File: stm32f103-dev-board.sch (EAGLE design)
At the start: 33 parts, among them Q1 8MHz, U1 STM32F103CBT6, U2 LM1117MP-3.3, Y1 32.768kHz

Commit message: v0.2
added led on PC13
added power led
added external power in
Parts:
- added D1, D2: (no value), SparkFun-LED:LED3MM
- added D3, D4: 1A/40V/500mV, SparkFun-DiscreteSemi:DIODE-SCHOTTKY-SS14
- added J5: (no value), SparkFun-Connectors:CONN_02
- added R1, R9: 470, rcl:R-EU_R0805
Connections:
- new net N$1: D3.A, X1.VBUS
- new net N$2: D2.A, R9.2
- new net N$3: D1.A, R1.2
- new net N$5: D4.A, J5.2
- net +3V3: now also R1.1
- net +5V: now also D3.C, D4.C; no longer X1.VBUS
- net GND: now also D1.C, D2.C, J5.1
- net PC13: now also R9.1
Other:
- note added: "Curious Mind http://acemielektronikci.blogspot.com"
- note added: "v0.2"
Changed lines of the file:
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@@
 <layer number="28" name="bValues" color="7" fill="1" visible="yes" active="no"/>
 <layer number="29" name="tStop" color="7" fill="3" visible="no" active="no"/>
-<layer number="30" name="bStop" color="7" fill="6" visible="no" active="no"/>
+<layer number="30" name="bStop" color="7" fill="1" visible="no" active="no"/>
 <layer number="31" name="tCream" color="7" fill="4" visible="no" active="no"/>
 <layer number="32" name="bCream" color="7" fill="5" visible="no" active="no"/>
@@
 <part name="J6" library="SparkFun-Connectors" deviceset="CONN_11" device=""/>
 <part name="J4" library="SparkFun-Connectors" deviceset="CONN_12" device=""/>
-<part name="FRAME1" library="SparkFun-Aesthetics" deviceset="FRAME-LETTER" device=""/>
+<part name="R1" library="rcl" deviceset="R-EU_" device="R0805" value="470"/>
+<part name="R9" library="rcl" deviceset="R-EU_" device="R0805" value="470"/>
+<part name="D1" library="SparkFun-LED" deviceset="LED" device="3MM"/>
+<part name="D2" library="SparkFun-LED" deviceset="LED" device="3MM"/>
+<part name="+3V4" library="supply1" deviceset="+3V3" device=""/>
+<part name="GND8" library="supply1" deviceset="GND" device=""/>
+<part name="D3" library="SparkFun-DiscreteSemi" deviceset="DIODE-SCHOTTKY" device="-SS14" value="1A/40V/500mV"/>
+<part name="D4" library="SparkFun-DiscreteSemi" deviceset="DIODE-SCHOTTKY" device="-SS14" value="1A/40V/500mV"/>
+<part name="J5" library="SparkFun-Connectors" deviceset="CONN_02" device=""/>
+<part name="GND11" library="supply1" deviceset="GND" device=""/>
+<part name="FRAME1" library="SparkFun-Aesthetics" deviceset="FRAME-LETTER" device="" value="FRAME-LETTER"/>
 </parts>
 <sheets>
@@
 <plain>
 <text x="-12.7" y="30.48" size="1.27" layer="91">BOOT1</text>
+<text x="30.48" y="-67.31" size="2.54" layer="91" font="vector">           Curious Mind
+http://acemielektronikci.blogspot.com</text>
+<text x="115.57" y="-67.056" size="2.54" layer="91" font="vector">v0.2</text>
 </plain>
 <instances>
@@
 <attribute name="VALUE" x="109.22" y="-25.4" size="1.778" layer="96"/>
 </instance>
-<instance part="P+2" gate="1" x="-83.82" y="-48.26" smashed="yes" rot="R180">
-<attribute name="VALUE" x="-81.28" y="-43.18" size="1.778" layer="96" rot="R270"/>
+<instance part="P+2" gate="1" x="-63.5" y="-48.26" smashed="yes" rot="R270">
+<attribute name="VALUE" x="-68.58" y="-45.72" size="1.778" layer="96"/>
 </instance>
 <instance part="P+3" gate="1" x="30.48" y="-5.08" smashed="yes">
@@
 <attribute name="VALUE" x="119.38" y="108.966" size="1.778" layer="96" font="vector" rot="R180"/>
 <attribute name="NAME" x="119.38" y="73.152" size="1.778" layer="95" font="vector" rot="R180"/>
+</instance>
+<instance part="R1" gate="G$1" x="-68.58" y="22.86" smashed="yes" rot="R180">
+<attribute name="NAME" x="-64.77" y="21.3614" size="1.778" layer="95" rot="R180"/>
+<attribute name="VALUE" x="-64.77" y="26.162" size="1.778" layer="96" rot="R180"/>
+</instance>
+<instance part="R9" gate="G$1" x="-68.58" y="15.24" smashed="yes" rot="R180">
+<attribute name="NAME" x="-64.77" y="13.7414" size="1.778" layer="95" rot="R180"/>
+<attribute name="VALUE" x="-64.77" y="18.542" size="1.778" layer="96" rot="R180"/>
+</instance>
+<instance part="D1" gate="G$1" x="-78.74" y="22.86" smashed="yes" rot="R270">
+<attribute name="NAME" x="-83.312" y="26.289" size="1.778" layer="95" font="vector"/>
+<attribute name="VALUE" x="-83.312" y="20.955" size="1.778" layer="96" font="vector" align="top-left"/>
+</instance>
+<instance part="D2" gate="G$1" x="-78.74" y="15.24" smashed="yes" rot="R270">
+<attribute name="NAME" x="-83.312" y="18.669" size="1.778" layer="95" font="vector"/>
+<attribute name="VALUE" x="-83.312" y="13.335" size="1.778" layer="96" font="vector" align="top-left"/>
+</instance>
+<instance part="+3V4" gate="G$1" x="-58.42" y="27.94" smashed="yes">
+<attribute name="VALUE" x="-60.96" y="22.86" size="1.778" layer="96" rot="R90"/>
+</instance>
+<instance part="GND8" gate="1" x="-86.36" y="12.7" smashed="yes">
+<attribute name="VALUE" x="-88.9" y="10.16" size="1.778" layer="96"/>
+</instance>
+<instance part="D3" gate="G$1" x="-83.82" y="-43.18" smashed="yes">
+<attribute name="NAME" x="-86.36" y="-41.148" size="1.778" layer="95" font="vector"/>
+<attribute name="VALUE" x="-86.36" y="-45.212" size="1.778" layer="96" font="vector" align="top-left"/>
+</instance>
+<instance part="D4" gate="G$1" x="-83.82" y="-53.34" smashed="yes">
+<attribute name="NAME" x="-86.36" y="-51.308" size="1.778" layer="95" font="vector"/>
+<attribute name="VALUE" x="-86.36" y="-55.372" size="1.778" layer="96" font="vector" align="top-left"/>
+</instance>
+<instance part="J5" gate="G$1" x="-93.98" y="-55.88" smashed="yes">
+<attribute name="VALUE" x="-96.52" y="-60.706" size="1.778" layer="96" font="vector"/>
+<attribute name="NAME" x="-96.52" y="-50.292" size="1.778" layer="95" font="vector"/>
+</instance>
+<instance part="GND11" gate="1" x="-83.82" y="-60.96" smashed="yes">
+<attribute name="VALUE" x="-86.36" y="-63.5" size="1.778" layer="96"/>
 </instance>
 <instance part="FRAME1" gate="G$1" x="-121.92" y="-73.66" smashed="yes"/>
@@
 <pinref part="J4" gate="G$1" pin="11"/>
 <wire x1="109.22" y1="78.74" x2="91.44" y2="78.74" width="0.1524" layer="91"/>
+</segment>
+<segment>
+<pinref part="D1" gate="G$1" pin="C"/>
+<pinref part="GND8" gate="1" pin="GND"/>
+<wire x1="-83.82" y1="22.86" x2="-86.36" y2="22.86" width="0.1524" layer="91"/>
+<wire x1="-86.36" y1="22.86" x2="-86.36" y2="15.24" width="0.1524" layer="91"/>
+<pinref part="D2" gate="G$1" pin="C"/>
+<wire x1="-83.82" y1="15.24" x2="-86.36" y2="15.24" width="0.1524" layer="91"/>
+<junction x="-86.36" y="15.24"/>
+</segment>
+<segment>
+<pinref part="J5" gate="G$1" pin="1"/>
+<wire x1="-86.36" y1="-55.88" x2="-83.82" y2="-55.88" width="0.1524" layer="91"/>
+<pinref part="GND11" gate="1" pin="GND"/>
+<wire x1="-83.82" y1="-55.88" x2="-83.82" y2="-58.42" width="0.1524" layer="91"/>
 </segment>
 </net>
@@
 <label x="-93.98" y="78.74" size="1.778" layer="95"/>
 </segment>
+<segment>
+<pinref part="R1" gate="G$1" pin="1"/>
+<wire x1="-63.5" y1="22.86" x2="-58.42" y2="22.86" width="0.1524" layer="91"/>
+<pinref part="+3V4" gate="G$1" pin="+3V3"/>
+<wire x1="-58.42" y1="22.86" x2="-58.42" y2="25.4" width="0.1524" layer="91"/>
+</segment>
 </net>
 <net name="N$7" class="0">
@@
 </segment>
 <segment>
-<pinref part="X1" gate="G$1" pin="VBUS"/>
+<pinref part="D3" gate="G$1" pin="C"/>
+<wire x1="-81.28" y1="-43.18" x2="-66.04" y2="-43.18" width="0.1524" layer="91"/>
+<wire x1="-66.04" y1="-43.18" x2="-66.04" y2="-48.26" width="0.1524" layer="91"/>
+<pinref part="D4" gate="G$1" pin="C"/>
+<wire x1="-66.04" y1="-48.26" x2="-66.04" y2="-53.34" width="0.1524" layer="91"/>
+<wire x1="-66.04" y1="-53.34" x2="-81.28" y2="-53.34" width="0.1524" layer="91"/>
 <pinref part="P+2" gate="1" pin="+5V"/>
-<wire x1="-86.36" y1="-43.18" x2="-83.82" y2="-43.18" width="0.1524" layer="91"/>
-<wire x1="-83.82" y1="-43.18" x2="-83.82" y2="-45.72" width="0.1524" layer="91"/>
+<junction x="-66.04" y="-48.26"/>
 </segment>
 </net>
@@
 <wire x1="-104.14" y1="76.2" x2="-83.82" y2="76.2" width="0.1524" layer="91"/>
 <label x="-93.98" y="76.2" size="1.778" layer="95"/>
+</segment>
+<segment>
+<pinref part="R9" gate="G$1" pin="1"/>
+<wire x1="-63.5" y1="15.24" x2="-58.42" y2="15.24" width="0.1524" layer="91"/>
+<label x="-63.5" y="15.24" size="1.778" layer="95"/>
 </segment>
 </net>
@@
 </segment>
 </net>
+<net name="N$2" class="0">
+<segment>
+<pinref part="R9" gate="G$1" pin="2"/>
+<pinref part="D2" gate="G$1" pin="A"/>
+<wire x1="-73.66" y1="15.24" x2="-76.2" y2="15.24" width="0.1524" layer="91"/>
+</segment>
+</net>
+<net name="N$3" class="0">
+<segment>
+<pinref part="R1" gate="G$1" pin="2"/>
+<pinref part="D1" gate="G$1" pin="A"/>
+<wire x1="-73.66" y1="22.86" x2="-76.2" y2="22.86" width="0.1524" layer="91"/>
+</segment>
+</net>
+<net name="N$1" class="0">
+<segment>
+<pinref part="X1" gate="G$1" pin="VBUS"/>
+<pinref part="D3" gate="G$1" pin="A"/>
+</segment>
+</net>
+<net name="N$5" class="0">
+<segment>
+<pinref part="J5" gate="G$1" pin="2"/>
+<pinref part="D4" gate="G$1" pin="A"/>
+</segment>
+</net>
 </nets>
 </sheet>
@@
 </schematic>
 </drawing>
+<compatibility>
+<note version="6.3" minversion="6.2.2" severity="warning">
+Since Version 6.2.2 text objects can contain more than one line,
+which will not be processed correctly with this version.
+</note>
+</compatibility>
 </eagle>

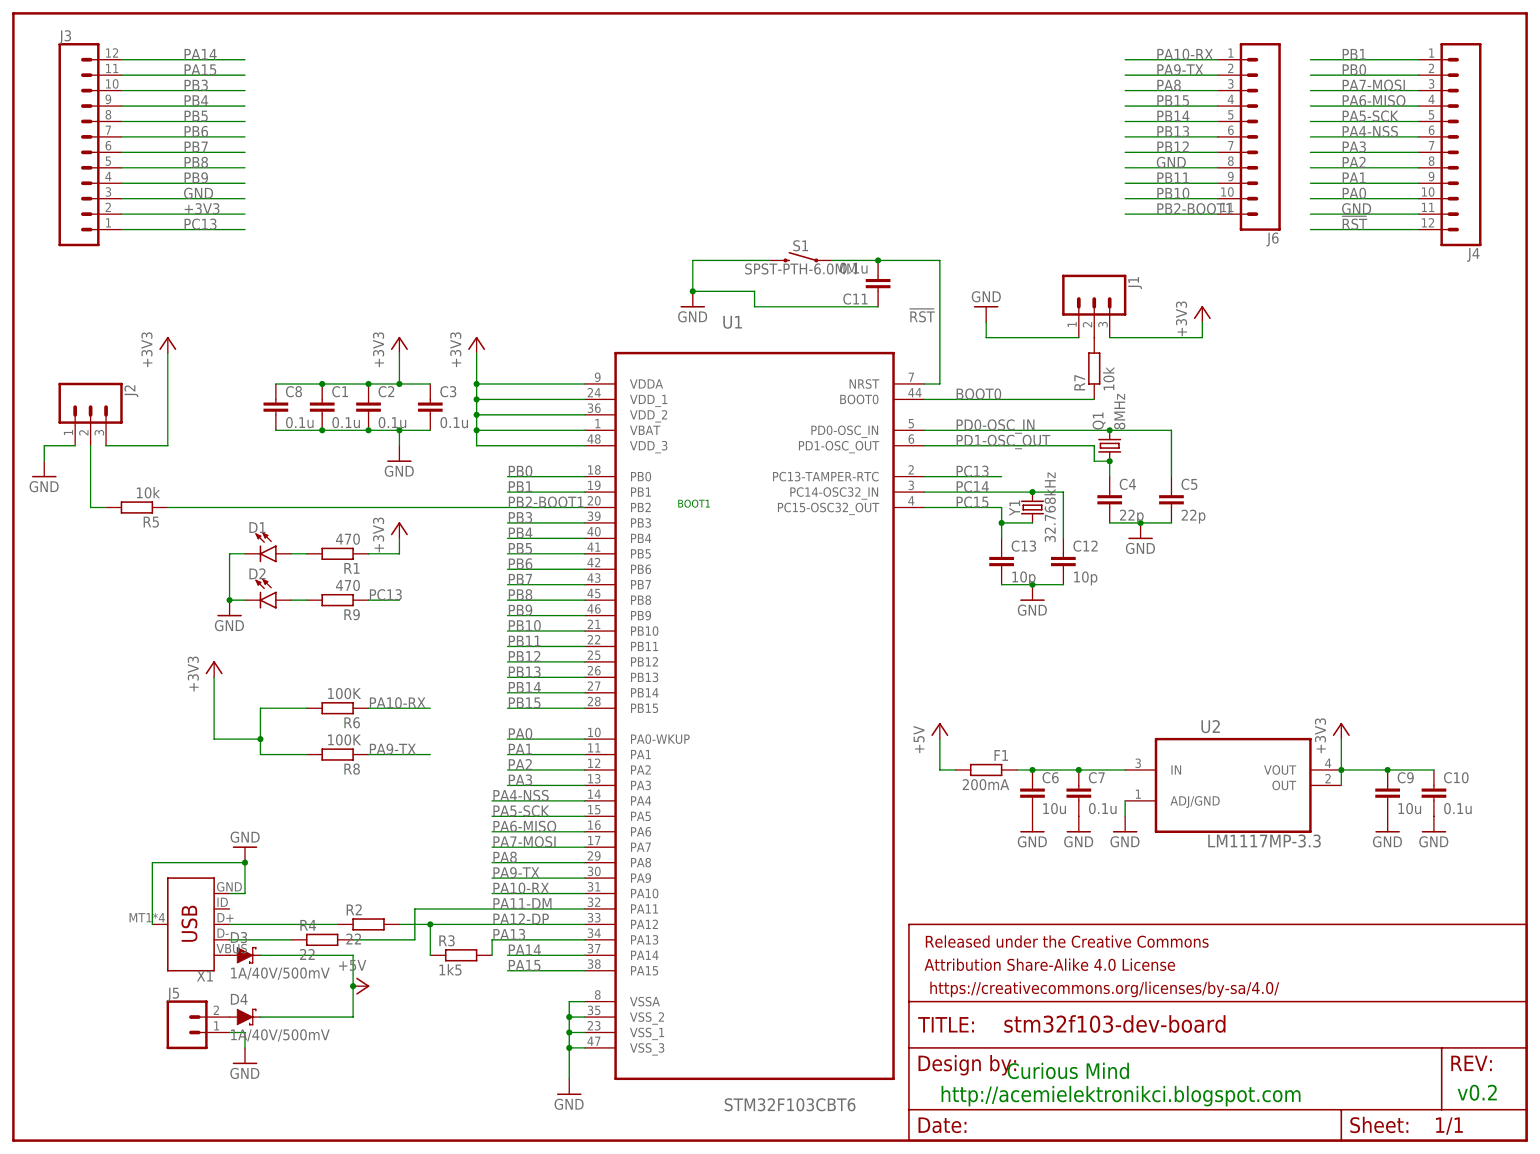
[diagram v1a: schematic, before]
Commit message: corrected usb pullup
corrected usb pullup
routed swdio (PA13)
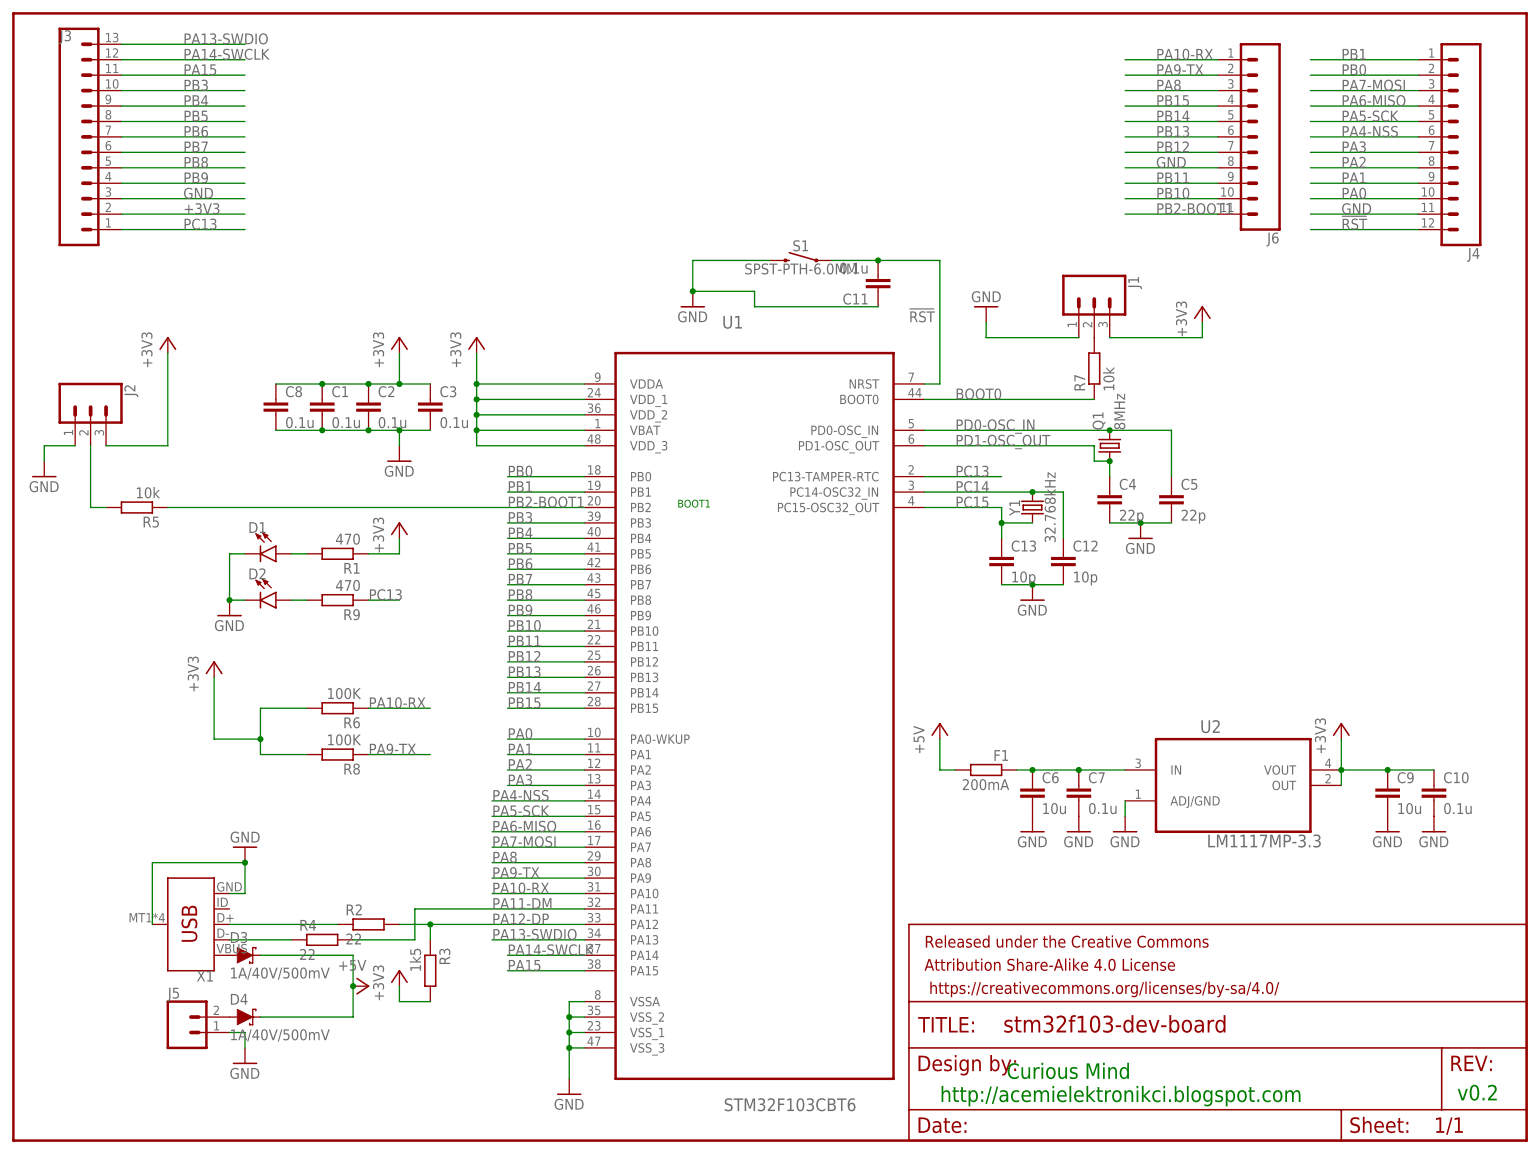
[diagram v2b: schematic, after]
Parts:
- J3: device SparkFun-Connectors:CONN_12 -> SparkFun-Connectors:CONN_13
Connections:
- net PA14 renamed PA14-SWCLK
- removed net PA13: R3.2, U1.PA13
- new net PA13-SWDIO: J3.13, U1.PA13
- net +3V3: now also R3.2
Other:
- moved on the sheet: R3
